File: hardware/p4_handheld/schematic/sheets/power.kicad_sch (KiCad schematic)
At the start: 0 parts

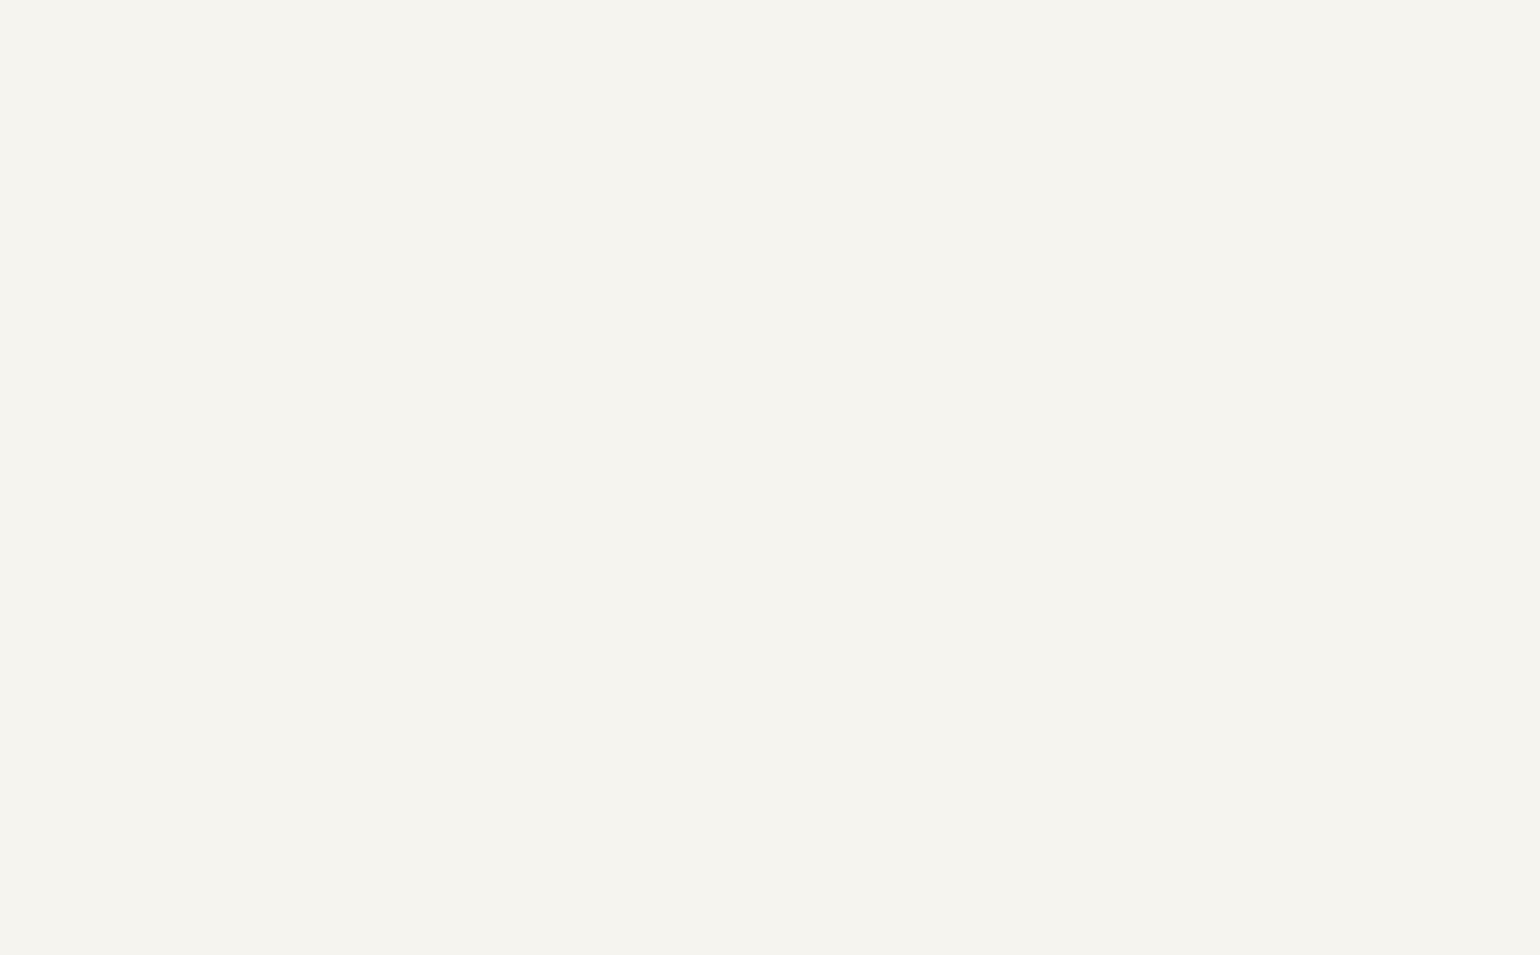
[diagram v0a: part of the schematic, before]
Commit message: hw(p4_handheld): power sheet connectivity
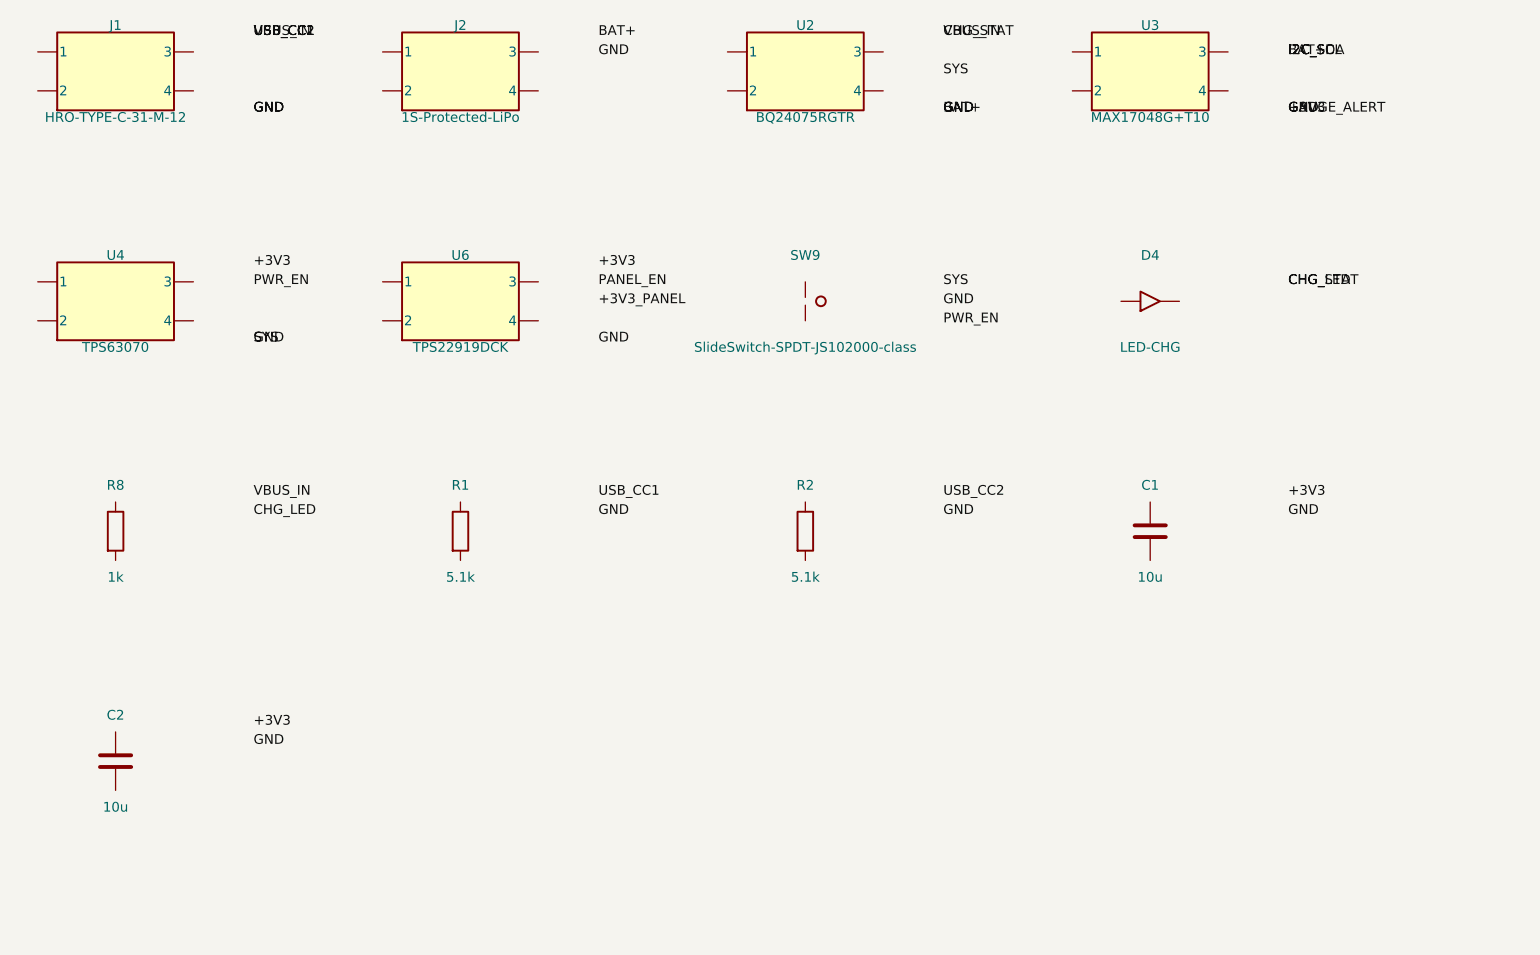
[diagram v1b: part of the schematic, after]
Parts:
- added C1, C2: 10u, C0603, symbol Device:C
- added D4: LED-CHG, LED0603-RD, symbol Device:LED
- added J1: HRO-TYPE-C-31-M-12, USB-C-SMD_TYPE-C-16PIN-2MD-073, symbol PSP4H:Block2
- added J2: 1S-Protected-LiPo, CONN-SMD_SM02B-SRSS-TB, symbol PSP4H:Block2
- added R1, R2: 5.1k, R0402, symbol Device:R
- added R8: 1k, R0402, symbol Device:R
- added SW9: SlideSwitch-SPDT-JS102000-class, SW-SMD_6P-L7.0-W3.5-P1.27-LS4.5-TL, symbol Switch:SW_Push
- added U2: BQ24075RGTR, QFN-16_L3.0-W3.0-P0.50-TL-EP1.7, symbol PSP4H:Block2
- added U3: MAX17048G+T10, TDFN-8_L2.0-W2.0-P0.50-BL-EP1.2, symbol PSP4H:Block2
- added U4: TPS63070, VQFN-HR-15_L3.0-W2.5-P0.50-BL_TPS63070RNMR, symbol PSP4H:Block2
- added U6: TPS22919DCK, SC-70-6_L2.2-W1.3-P0.65-LS2.1-BR, symbol PSP4H:Block2

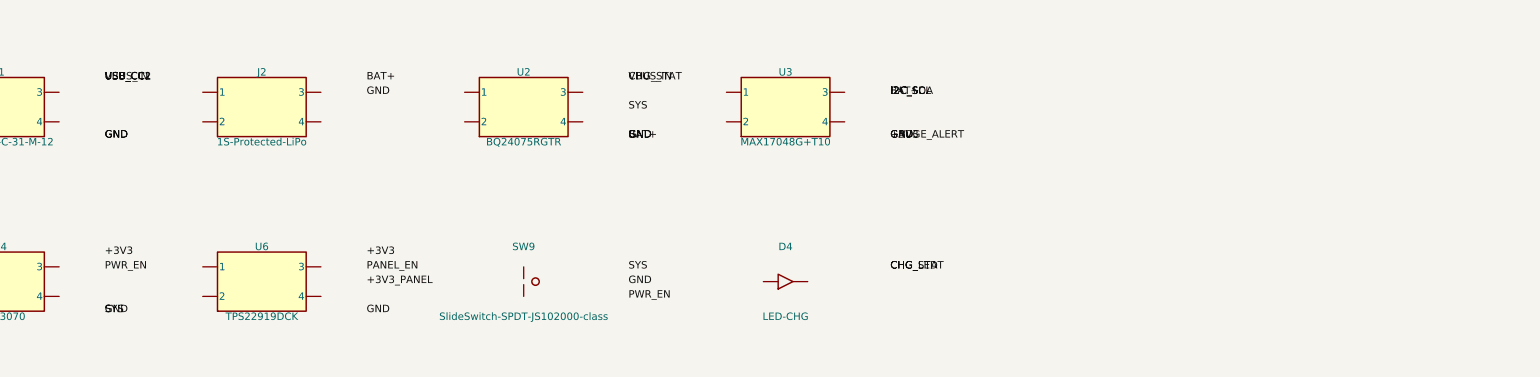
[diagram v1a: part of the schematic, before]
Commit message: hw(p4_handheld): compute cluster ported, diffs clean vs card
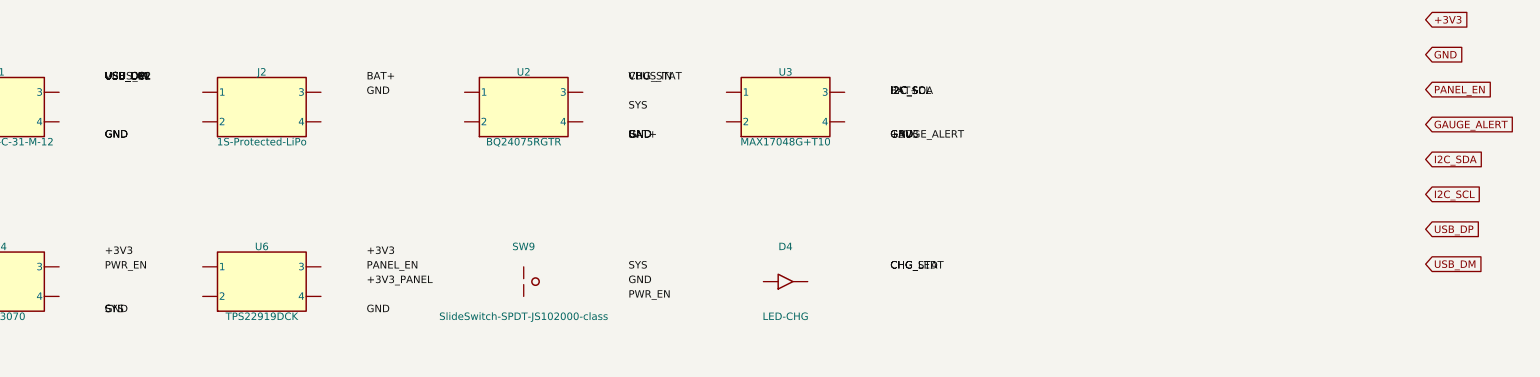
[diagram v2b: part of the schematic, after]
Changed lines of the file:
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@@
   (label "USB_CC2" (at 53 30 0) (fields_autoplaced)
     (effects (font (size 1.27 1.27)) (justify left)))
+  (label "USB_DP" (at 53 30 0) (fields_autoplaced)
+    (effects (font (size 1.27 1.27)) (justify left)))
+  (label "USB_DM" (at 53 30 0) (fields_autoplaced)
+    (effects (font (size 1.27 1.27)) (justify left)))
   (symbol (lib_id "PSP4H:Block2") (at 80 35 0) (unit 1)
     (exclude_from_sim no) (in_bom yes) (on_board yes) (dnp no) (fields_autoplaced)
@@
   (label "GND" (at 53 122.5 0) (fields_autoplaced)
     (effects (font (size 1.27 1.27)) (justify left)))
+  (global_label "+3V3" (shape input) (at 280 20 0) (fields_autoplaced)
+    (effects (font (size 1.27 1.27)) (justify left))
+    (property "Intersheetrefs" "${INTERSHEET_REFS}" (at 280 20 0)
+      (effects (font (size 1.27 1.27)) hide))
+  )
+  (global_label "GND" (shape input) (at 280 26 0) (fields_autoplaced)
+    (effects (font (size 1.27 1.27)) (justify left))
+    (property "Intersheetrefs" "${INTERSHEET_REFS}" (at 280 26 0)
+      (effects (font (size 1.27 1.27)) hide))
+  )
+  (global_label "PANEL_EN" (shape input) (at 280 32 0) (fields_autoplaced)
+    (effects (font (size 1.27 1.27)) (justify left))
+    (property "Intersheetrefs" "${INTERSHEET_REFS}" (at 280 32 0)
+      (effects (font (size 1.27 1.27)) hide))
+  )
+  (global_label "GAUGE_ALERT" (shape input) (at 280 38 0) (fields_autoplaced)
+    (effects (font (size 1.27 1.27)) (justify left))
+    (property "Intersheetrefs" "${INTERSHEET_REFS}" (at 280 38 0)
+      (effects (font (size 1.27 1.27)) hide))
+  )
+  (global_label "I2C_SDA" (shape input) (at 280 44 0) (fields_autoplaced)
+    (effects (font (size 1.27 1.27)) (justify left))
+    (property "Intersheetrefs" "${INTERSHEET_REFS}" (at 280 44 0)
+      (effects (font (size 1.27 1.27)) hide))
+  )
+  (global_label "I2C_SCL" (shape input) (at 280 50 0) (fields_autoplaced)
+    (effects (font (size 1.27 1.27)) (justify left))
+    (property "Intersheetrefs" "${INTERSHEET_REFS}" (at 280 50 0)
+      (effects (font (size 1.27 1.27)) hide))
+  )
+  (global_label "USB_DP" (shape input) (at 280 56 0) (fields_autoplaced)
+    (effects (font (size 1.27 1.27)) (justify left))
+    (property "Intersheetrefs" "${INTERSHEET_REFS}" (at 280 56 0)
+      (effects (font (size 1.27 1.27)) hide))
+  )
+  (global_label "USB_DM" (shape input) (at 280 62 0) (fields_autoplaced)
+    (effects (font (size 1.27 1.27)) (justify left))
+    (property "Intersheetrefs" "${INTERSHEET_REFS}" (at 280 62 0)
+      (effects (font (size 1.27 1.27)) hide))
+  )
   (symbol (lib_id "power:+3V3") (at 280 260 0) (unit 1) (exclude_from_sim no) (in_bom yes) (on_board yes)
  (property "Reference" "#PWR01" (at 280 256 0) (effects (font (size 1.27 1.27)) hide))

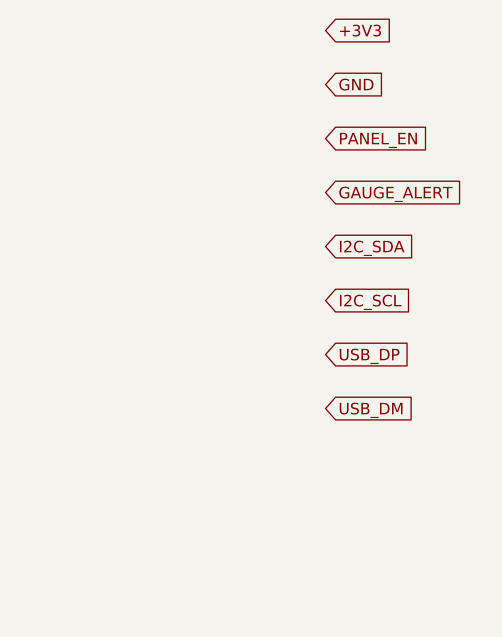
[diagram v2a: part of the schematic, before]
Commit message: hw(p4_handheld): display sheet wired to Waveshare 2.8in DSI panel
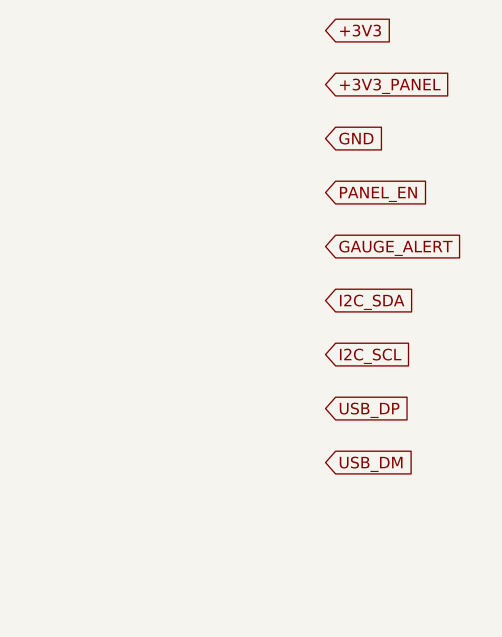
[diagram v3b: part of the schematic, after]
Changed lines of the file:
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@@
       (effects (font (size 1.27 1.27)) hide))
   )
-  (global_label "GND" (shape input) (at 280 26 0) (fields_autoplaced)
+  (global_label "+3V3_PANEL" (shape input) (at 280 26 0) (fields_autoplaced)
     (effects (font (size 1.27 1.27)) (justify left))
     (property "Intersheetrefs" "${INTERSHEET_REFS}" (at 280 26 0)
       (effects (font (size 1.27 1.27)) hide))
   )
-  (global_label "PANEL_EN" (shape input) (at 280 32 0) (fields_autoplaced)
+  (global_label "GND" (shape input) (at 280 32 0) (fields_autoplaced)
     (effects (font (size 1.27 1.27)) (justify left))
     (property "Intersheetrefs" "${INTERSHEET_REFS}" (at 280 32 0)
       (effects (font (size 1.27 1.27)) hide))
   )
-  (global_label "GAUGE_ALERT" (shape input) (at 280 38 0) (fields_autoplaced)
+  (global_label "PANEL_EN" (shape input) (at 280 38 0) (fields_autoplaced)
     (effects (font (size 1.27 1.27)) (justify left))
     (property "Intersheetrefs" "${INTERSHEET_REFS}" (at 280 38 0)
       (effects (font (size 1.27 1.27)) hide))
   )
-  (global_label "I2C_SDA" (shape input) (at 280 44 0) (fields_autoplaced)
+  (global_label "GAUGE_ALERT" (shape input) (at 280 44 0) (fields_autoplaced)
     (effects (font (size 1.27 1.27)) (justify left))
     (property "Intersheetrefs" "${INTERSHEET_REFS}" (at 280 44 0)
       (effects (font (size 1.27 1.27)) hide))
   )
-  (global_label "I2C_SCL" (shape input) (at 280 50 0) (fields_autoplaced)
+  (global_label "I2C_SDA" (shape input) (at 280 50 0) (fields_autoplaced)
     (effects (font (size 1.27 1.27)) (justify left))
     (property "Intersheetrefs" "${INTERSHEET_REFS}" (at 280 50 0)
       (effects (font (size 1.27 1.27)) hide))
   )
-  (global_label "USB_DP" (shape input) (at 280 56 0) (fields_autoplaced)
+  (global_label "I2C_SCL" (shape input) (at 280 56 0) (fields_autoplaced)
     (effects (font (size 1.27 1.27)) (justify left))
     (property "Intersheetrefs" "${INTERSHEET_REFS}" (at 280 56 0)
       (effects (font (size 1.27 1.27)) hide))
   )
-  (global_label "USB_DM" (shape input) (at 280 62 0) (fields_autoplaced)
+  (global_label "USB_DP" (shape input) (at 280 62 0) (fields_autoplaced)
     (effects (font (size 1.27 1.27)) (justify left))
     (property "Intersheetrefs" "${INTERSHEET_REFS}" (at 280 62 0)
       (effects (font (size 1.27 1.27)) hide))
   )
+  (global_label "USB_DM" (shape input) (at 280 68 0) (fields_autoplaced)
+    (effects (font (size 1.27 1.27)) (justify left))
+    (property "Intersheetrefs" "${INTERSHEET_REFS}" (at 280 68 0)
+      (effects (font (size 1.27 1.27)) hide))
+  )
